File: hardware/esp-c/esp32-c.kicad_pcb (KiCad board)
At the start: 2 copper layers, 70.5 x 64 mm, 76 parts, among them U1 MCP23008-E/ML, U10 HC-FPC-05-09-10RLTAG, U11 HC-FPC-05-09-10RLTAG, U12 ESP32-WROOM-32E(4MB), U13 AFC42-S14FMA-1H, U2 CH340C_C7464026, U3 SS8050_C2150, U4 MCP23008-E/ML, U5 MCP42010T-I/SL, U6 HC-FPC-05-09-10RLTAG, U7 IPFP051A30472R5, U8 SS8050_C2150, U9 AMS1117-3_3

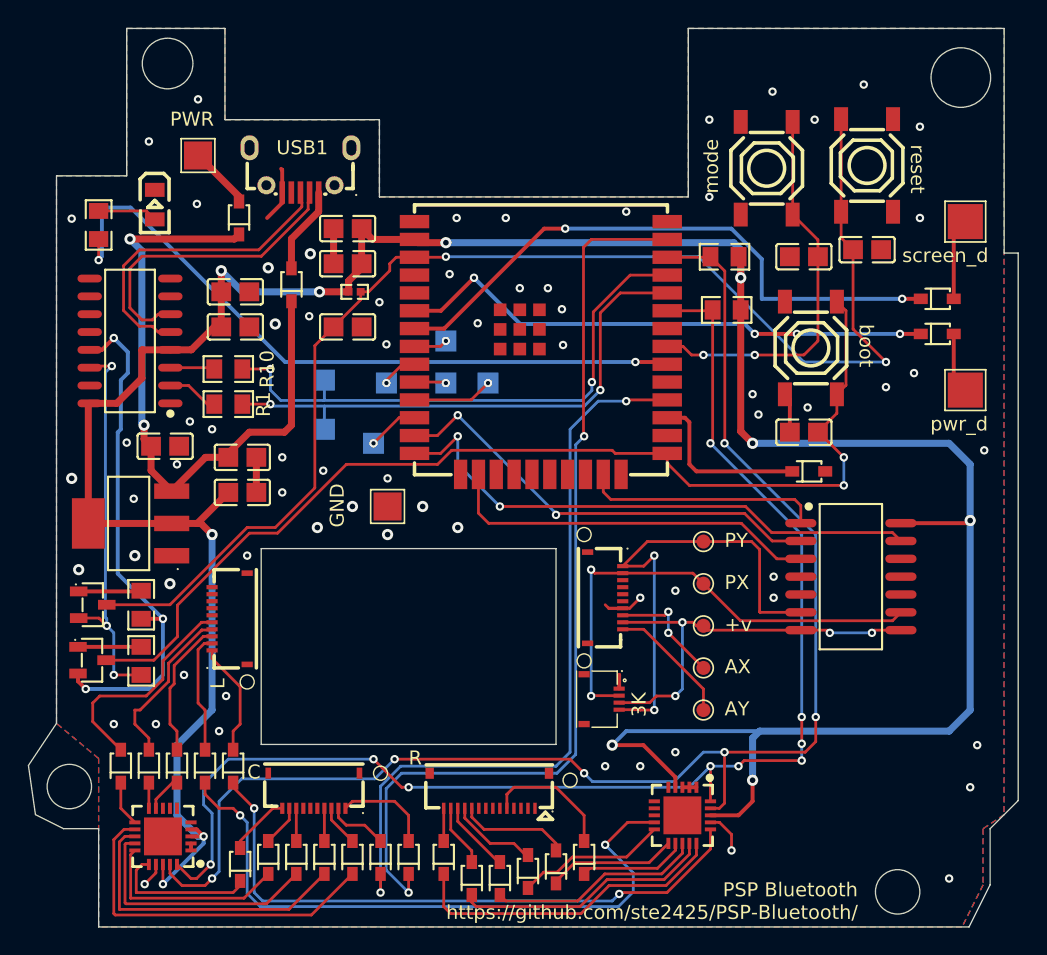
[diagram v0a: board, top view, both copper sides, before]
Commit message: [Hardware] Added LED pad and changed switch to right angle
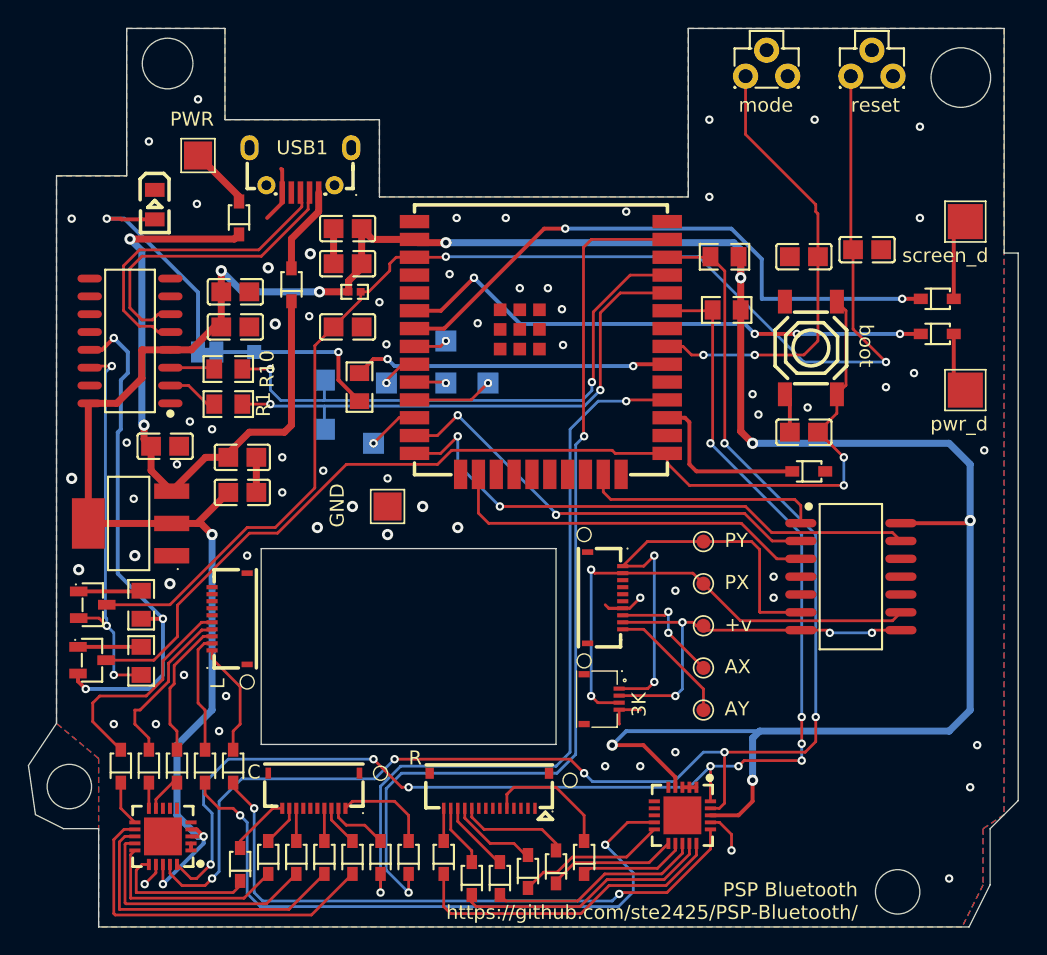
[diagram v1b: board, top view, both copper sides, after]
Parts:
- removed MODE1, RESET1: TS-1187A-B-A-B, JLCPCB_footprint:SW-SMD_4P-L5.1-W5.1-P3.70-LS6.5-TL-2
- added JP1: SolderJumper_2_Bridged, Jumper:SolderJumper-2_P1.3mm_Bridged_Pad1.0x1.5mm, B.Cu at (115.2, 94.0)
- added TP9: TestPoint, TestPoint:TestPoint_Pad_1.0x1.0mm, B.Cu at (118.5, 94.0)
- added U14: TC1109DE26048, JLCPCB_footprint:SW-TH_3P-L4.5-W4.5-P1.8-LS3.0, F.Cu at (155.0, 73.4)
- added U15: TC1109DE26048, JLCPCB_footprint:SW-TH_3P-L4.5-W4.5-P1.8-LS3.0, F.Cu at (162.5, 73.4)
- moved R9 21.9 mm to (126.0, 96.5), turned to 90 degrees
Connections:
- LED1 pad 1: Net-(LED1-+) -> Net-(JP1-A)
- R9 pad 1: Net-(LED1-+) -> Net-(JP1-B)
- U7 pad 1: GND -> /PSP Pins 2K/PSP_y
- U7 pad 2: /PSP Pins 2K/PSP_x -> /PSP Pins 2K/+V
- U7 pad 3: /PSP Pins 2K/+V -> /PSP Pins 2K/PSP_x
- U7 pad 4: /PSP Pins 2K/PSP_y -> GND
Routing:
- net /ESP32/LEDIndicator: track 50.2 -> 22.6 mm
- net Net-(JP1-A): track 0.00 -> 16.4 mm, vias 0 -> 1
- net Net-(JP1-B): track 0.00 -> 12.6 mm, vias 0 -> 1
- net /ESP32/ESP_MODE: track 27.7 -> 32.4 mm
- net Net-(LED1-+): track 4.25 -> 0.00 mm
- net /ESP32/ESP_EN: track 94.1 -> 96.8 mm
- net /PSP Pins 2K/PSP_y: track 34.2 -> 32.4 mm
- net GND: track 23.4 -> 25.0 mm, vias 68 -> 66
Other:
- board text added: "LED"
